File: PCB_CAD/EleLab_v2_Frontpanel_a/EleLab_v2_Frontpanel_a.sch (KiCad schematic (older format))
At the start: 28 parts, among them J1 Conn_01x04, J10 Conn_01x01, J11 Conn_01x01, J12 Conn_01x01, J13 VBUS, J14 D+, J15 D-, J16 GND, J17 VBUS, J18 D+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

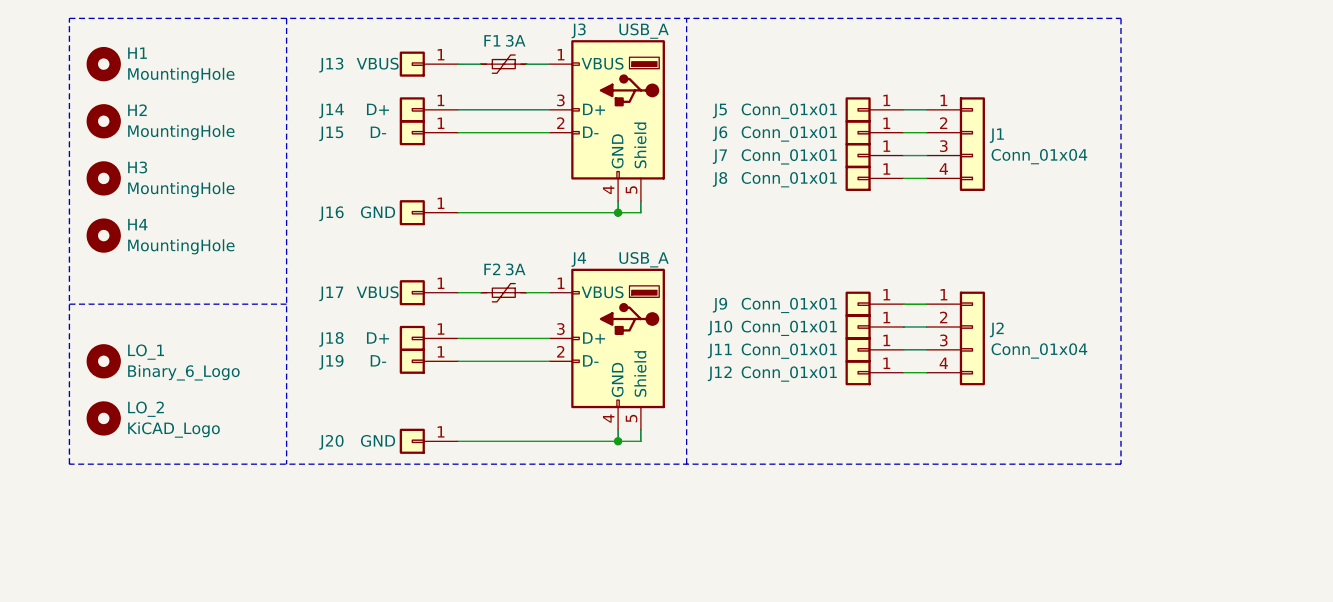
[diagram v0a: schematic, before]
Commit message: Add files via upload
Made STEP of all files, added more fans and vents to variable PSU, Added iOS charging support to the front panel board, created STLs for the variable power supply. Added model for USB ports.
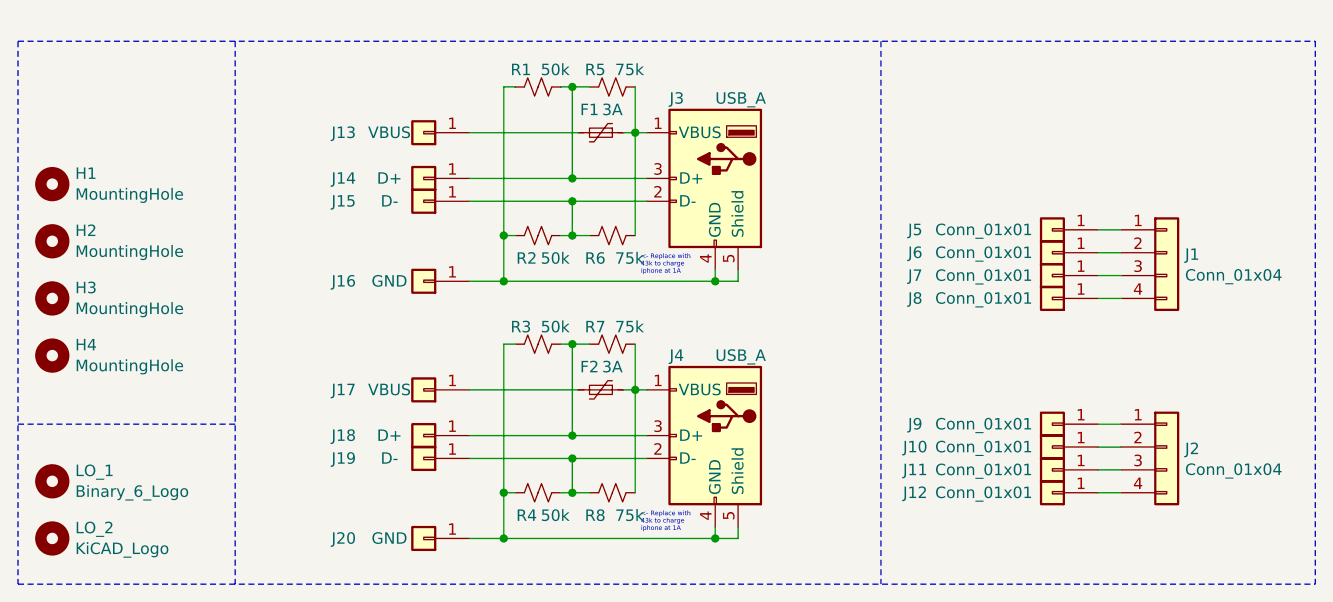
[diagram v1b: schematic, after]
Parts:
- added R1, R2, R3, R4: 50k, Resistor_THT:R_Axial_DIN0204_L3.6mm_D1.6mm_P7.62mm_Horizontal, symbol Device:R_Small_US
- added R5, R6, R7, R8: 75k, Resistor_THT:R_Axial_DIN0204_L3.6mm_D1.6mm_P7.62mm_Horizontal, symbol Device:R_Small_US
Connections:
- net at F1.1, J3.1 (VBUS): now also R5.2, R6.2
- net at J15.1 (Pin_1), J3.2 (D-): now also R2.2, R6.1
- net at J14.1 (Pin_1), J3.3 (D+): now also R1.2, R5.1
- net at J16.1 (Pin_1), J3.4 (GND), J3.5 (Shield): now also R1.1, R2.1
- net at F2.1, J4.1 (VBUS): now also R7.2, R8.2
- net at J19.1 (Pin_1), J4.2 (D-): now also R4.2, R8.1
- net at J18.1 (Pin_1), J4.3 (D+): now also R3.2, R7.1
- net at J20.1 (Pin_1), J4.4 (GND), J4.5 (Shield): now also R3.1, R4.1
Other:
- note added: "<- Replace with \n43k to charge \niphone at 1A"
- moved on the sheet: F1, H1, H2, H3, H4, J1, J10, J11, J12, J13, J14, J15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
